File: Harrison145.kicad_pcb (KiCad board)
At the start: 2 copper layers, 148 parts, among them J1 Pitch_ANT, J2 VOL_ANTENNA, J3 M3_PTH, J4 M3_PTH, Q1 MMBT3906, Q10 SMP5484, Q11 MMBT3906, Q12 MMBT3906, Q13 SMP5484, Q14 MMBT3904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

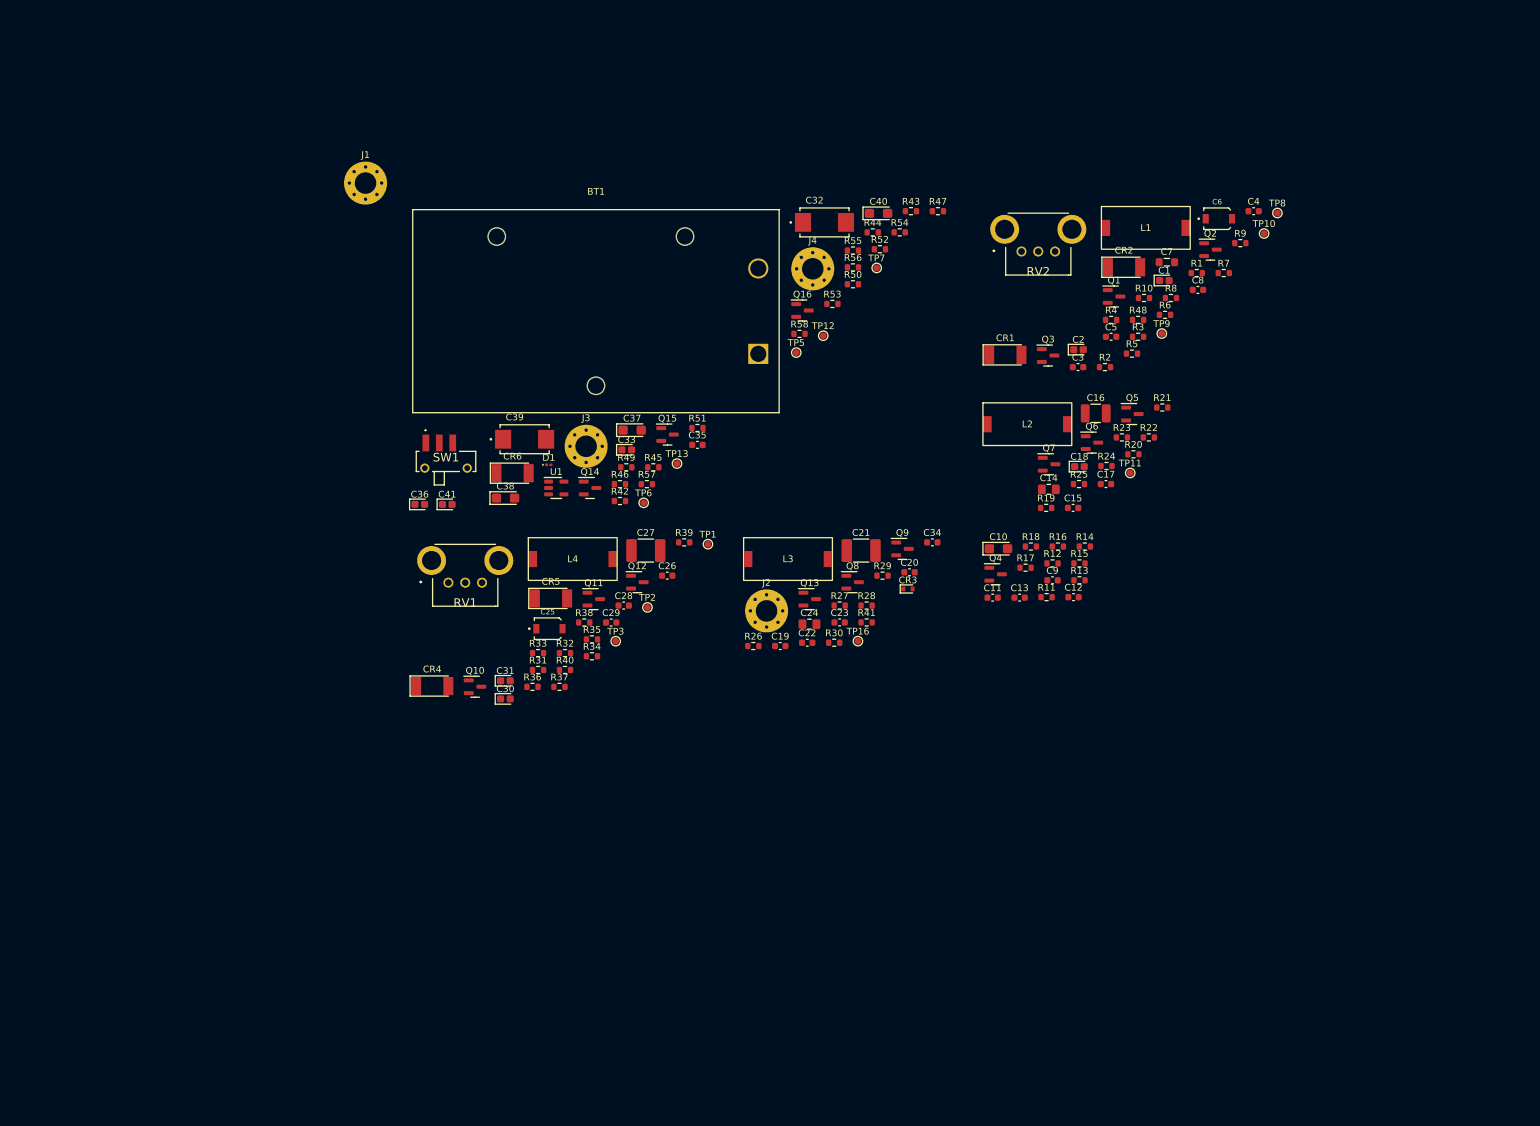
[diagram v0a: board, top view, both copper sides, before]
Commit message: Components mostly placed
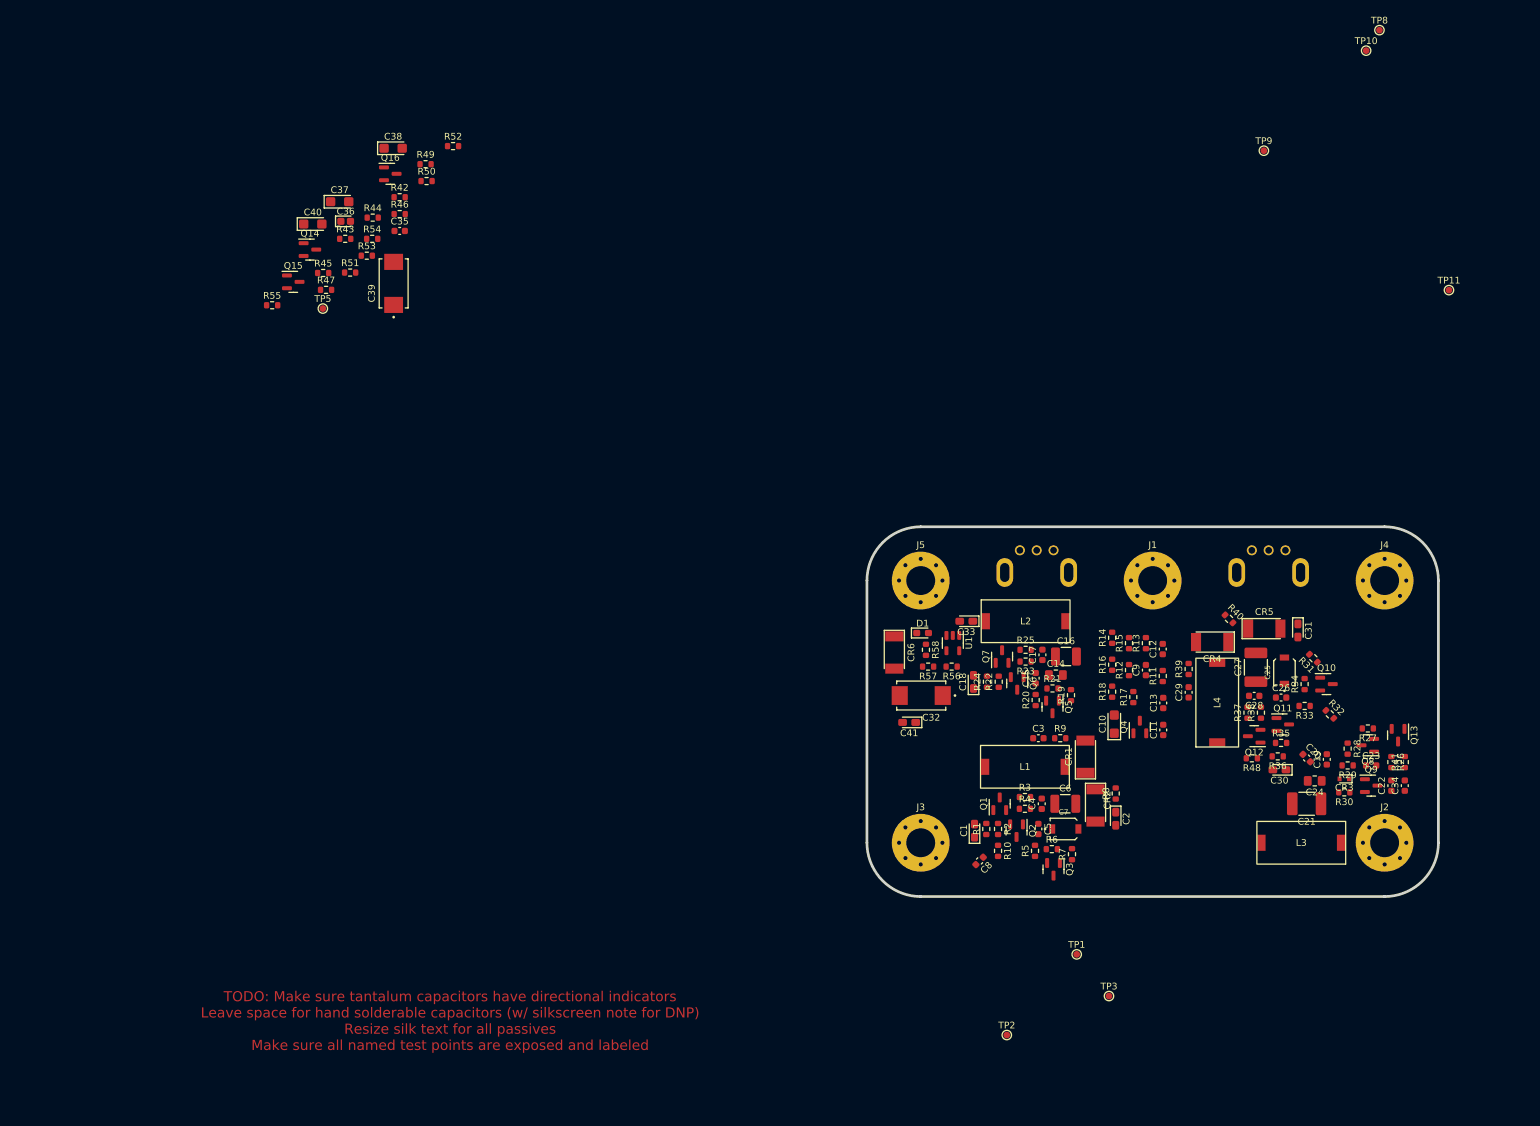
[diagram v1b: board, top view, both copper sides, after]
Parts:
- removed BT1: +9V, Battery:BatteryHolder_Eagle_12BH611-GR
- removed SW1: SW_SPDT, Theremin:CSS1210TB
- removed TP12, TP13, TP16, TP6, TP7: TestPoint, TestPoint:TestPoint_Pad_D1.0mm
- added J5: 9V IN, MountingHole:MountingHole_4.3mm_M4_Pad_Via, F.Cu at (141.0, 115.0)
- C1, C18, C2, C30, C31, C33, C41: footprint Capacitor_Tantalum_SMD:CP_EIA-1608-08_AVX-J -> Capacitor_Tantalum_SMD:CP_EIA-2012-12_Kemet-R_Pad1.30x1.05mm_HandSolder
- C11, C12, C13, C9: value .01uF -> 0.01uF
- C6: footprint Theremin:CAPV_JZ400 -> Capacitor_SMD:C_1210_3225Metric_Pad1.33x2.70mm_HandSolder
- C7: footprint Inductor_SMD:L_0805_2012Metric_Pad1.05x1.20mm_HandSolder -> Theremin:CAPV_JZ400
- D1: footprint LED_SMD:LED_0201_0603Metric -> LED_SMD:LED_0603_1608Metric_Pad1.05x0.95mm_HandSolder
- J1: value Pitch_ANT -> PITCH ANTENNA; footprint MountingHole:MountingHole_3.2mm_M3_Pad_Via -> MountingHole:MountingHole_4.3mm_M4_Pad_Via
- J2: value VOL_ANTENNA -> VOLUME ANTENNA; footprint MountingHole:MountingHole_3.2mm_M3_Pad_Via -> MountingHole:MountingHole_4.3mm_M4_Pad_Via
- J3: value M3_PTH -> GROUND POINT; footprint MountingHole:MountingHole_3.2mm_M3_Pad_Via -> MountingHole:MountingHole_4.3mm_M4_Pad_Via
- J4: value M3_PTH -> LINE OUT; footprint MountingHole:MountingHole_3.2mm_M3_Pad_Via -> MountingHole:MountingHole_4.3mm_M4_Pad_Via
- RV1, RV2: moved to B.Cu
- moved J1 131.2 mm to (175.5, 115.0)
- moved Q10 126.6 mm to (201.4, 130.4)
- moved RV1 122.1 mm to (192.8, 110.5)
- moved C31 118.1 mm to (197.1, 122.4), turned to -90 degrees
- moved CR4 116.2 mm to (184.4, 124.2), turned to 180 degrees
- moved C30 115.6 mm to (194.4, 143.1), turned to 180 degrees
- moved R31 115.3 mm to (199.4, 126.5), turned to 135 degrees
- moved R33 114.3 mm to (198.1, 133.6), turned to 180 degrees
- moved R32 114.1 mm to (201.9, 134.9), turned to -45 degrees
- moved R36 111.3 mm to (194.1, 141.1), turned to 180 degrees
- moved C25 109.5 mm to (195.1, 128.4), turned to 90 degrees
- moved CR5 106.2 mm to (192.1, 122.2)
- moved R34 106.1 mm to (198.1, 130.4), turned to 90 degrees
- moved Q11 104.2 mm to (194.9, 136.4)
- moved R35 103.7 mm to (194.6, 139.2)
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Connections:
- Q13 pad 1: E -> C
- Q13 pad 2: C -> E
- Q5 pad 1: +7.5V -> B
- Q5 pad 2: B -> +7.5V
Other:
- board outline added: 85 x 55 mm
- board text added: "TODO: Make sure tantalum capacitors have directional indicators Leave space for hand solderable capacitors (w/ silkscreen note for DNP) Resize silk text for all passives Make sure all named test points are exposed and labeled"

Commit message: Revisions
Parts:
- moved TP5 181.8 mm to (229.5, 114.4)
- moved R55 163.6 mm to (201.2, 121.2)
- moved C40 161.8 mm to (199.9, 124.4), turned to 90 degrees
- moved Q15 161.3 mm to (197.2, 131.2), turned to -90 degrees
- moved R51 158.4 mm to (203.2, 128.2), turned to 180 degrees
- moved C37 157.7 mm to (196.2, 127.9), turned to 180 degrees
- moved Q16 157.3 mm to (203.3, 123.8), turned to 180 degrees
- moved R49 156.1 mm to (203.1, 130.0), turned to 180 degrees
- moved Q14 153.1 mm to (195.0, 115.3), turned to -90 degrees
- moved R45 152.5 mm to (197.6, 115.0), turned to -90 degrees
- moved R52 152.1 mm to (203.2, 126.4), turned to 180 degrees
- moved R50 151.9 mm to (200.5, 128.8), turned to 90 degrees
- moved C38 150.8 mm to (194.2, 124.2), turned to -90 degrees
- moved R53 150.6 mm to (197.1, 125.7), turned to 180 degrees
- moved R54 149.8 mm to (197.2, 123.1), turned to -135 degrees
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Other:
- board text added: "TODO: Make sure tantalum capacitors have directional indicators Leave space for hand solderable capacitors (w/ silkscreen note for DNP) Resize silk text for all passives Scoot volume knob away from edge Hook test points for everything specified as needing scope connections Make sure layout still makes sense with double plate configuration Make sure all named test points are exposed and labeled Ge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"
- board text removed: "TODO: Make sure tantalum capacitors have directional indicators Leave space for hand solderable capacitors (w/ silkscreen note for DNP) Resize silk text for all passives Make sure all named test points are exposed and labeled"

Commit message: Better component placements
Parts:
- removed TP10, TP11, TP9: TestPoint, TestPoint:TestPoint_Pad_D1.0mm
- added C14_TEST1: C, Capacitor_THT:C_Disc_D3.0mm_W1.6mm_P2.50mm, F.Cu at (163.4, 110.4)
- added C24_TEST1: C, Capacitor_THT:C_Disc_D3.0mm_W1.6mm_P2.50mm, F.Cu at (195.9, 158.4)
- added JP1: A, Jumper:SolderJumper-2_P1.3mm_Open_RoundedPad1.0x1.5mm, F.Cu at (147.3, 140.3)
- added JP2: B, Jumper:SolderJumper-2_P1.3mm_Open_RoundedPad1.0x1.5mm, F.Cu at (162.3, 127.5)
- added JP3: C, Jumper:SolderJumper-2_P1.3mm_Open_RoundedPad1.0x1.5mm, F.Cu at (182.6, 148.4)
- added JP4: D, Jumper:SolderJumper-2_P1.3mm_Open_RoundedPad1.0x1.5mm, F.Cu at (186.6, 145.7)
- added JP5: E, Jumper:SolderJumper-2_P1.3mm_Open_RoundedPad1.0x1.5mm, F.Cu at (195.1, 139.9)
- added JP6: F, Jumper:SolderJumper-2_P1.3mm_Open_RoundedPad1.0x1.5mm, F.Cu at (168.5, 139.0)
- added TP4: TestPoint, TestPoint:TestPoint_Loop_D1.80mm_Drill1.0mm_Beaded, F.Cu at (175.4, 146.6)
- added TP6: TestPoint, TestPoint:TestPoint_Loop_D1.80mm_Drill1.0mm_Beaded, F.Cu at (210.5, 145.7)
- added TP7: TestPoint, TestPoint:TestPoint_Loop_D1.80mm_Drill1.0mm_Beaded, F.Cu at (186.0, 117.0)
- TP1, TP2, TP3, TP5, TP8: footprint TestPoint:TestPoint_Pad_D1.0mm -> TestPoint:TestPoint_Loop_D1.80mm_Drill1.0mm_Beaded
- moved TP8 104.2 mm to (200.5, 137.0)
- moved TP3 44.8 mm to (138.0, 144.5)
- moved TP1 27.6 mm to (189.5, 159.5)
- moved TP2 24.3 mm to (161.5, 159.5)
- moved TP5 20.6 mm to (210.5, 122.4)
- moved R48 18.8 mm to (203.1, 131.9), turned to 0 degrees
- moved C14 18.1 mm to (166.6, 110.4), turned to 0 degrees
- moved C16 13.8 mm to (166.8, 114.4), turned to 90 degrees
- moved C24 13.1 mm to (201.8, 158.4), turned to 0 degrees
- moved R8 9.54 mm to (145.3, 149.4), turned to -90 degrees
- moved C2 9.30 mm to (145.3, 145.6), turned to 90 degrees
- moved R9 8.99 mm to (153.2, 158.0), turned to 180 degrees
- moved C21 8.67 mm to (201.8, 153.8), turned to -90 degrees
- moved CR1 8.66 mm to (149.8, 154.9), turned to -90 degrees
- moved C3 8.35 mm to (156.4, 158.0), turned to 180 degrees
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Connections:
- C13 pad 2: C -> Net-(C13-Pad2)
- C35 pad 1: E -> Net-(C35-Pad1)
- C8 pad 2: F -> Net-(C8-Pad2)
- Q10 pad 1: D -> Net-(Q10-Pad1)
- R11 pad 1: A -> Net-(R11-Pad1)
- R17 pad 2: C -> Net-(C13-Pad2)
- R18 pad 2: B -> Net-(R18-Pad2)
- R31 pad 1: D -> Net-(Q10-Pad1)
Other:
- board text added: "AMP"
- board text added: "FPO"
- board text added: "FVO"
- board text added: "MIX"
- board text added: "TODO: Make sure tantalum capacitors have directional indicators Buy test points and standoffs Resize silk text for all passives Scoot volume knob away from edge Hook test points for everything specified as needing scope connections Make sure layout still makes sense with double plate configuration Make sure all named test points are exposed and labeled Generate annotated BOM and attach datasheets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"
- board text added: "VPO"
- board text added: "VVO"
- board text removed: "TODO: Make sure tantalum capacitors have directional indicators Leave space for hand solderable capacitors (w/ silkscreen note for DNP) Resize silk text for all passives Scoot volume knob away from edge Hook test points for everything specified as needing scope connections Make sure layout still makes sense with double plate configuration Make sure all named test points are exposed and labeled Ge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"
